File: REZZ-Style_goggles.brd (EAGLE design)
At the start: 65.5 x 65.5 mm, 85 parts

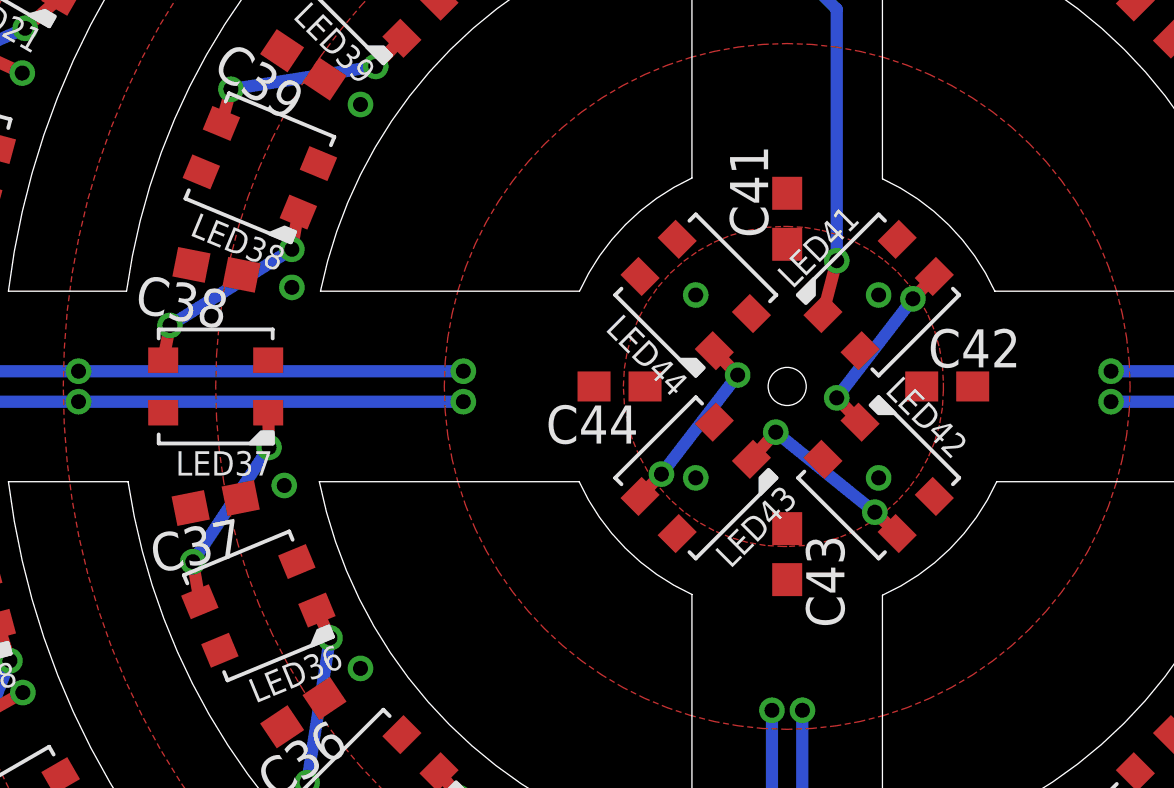
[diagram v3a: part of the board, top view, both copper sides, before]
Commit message: revised placements to improve pours
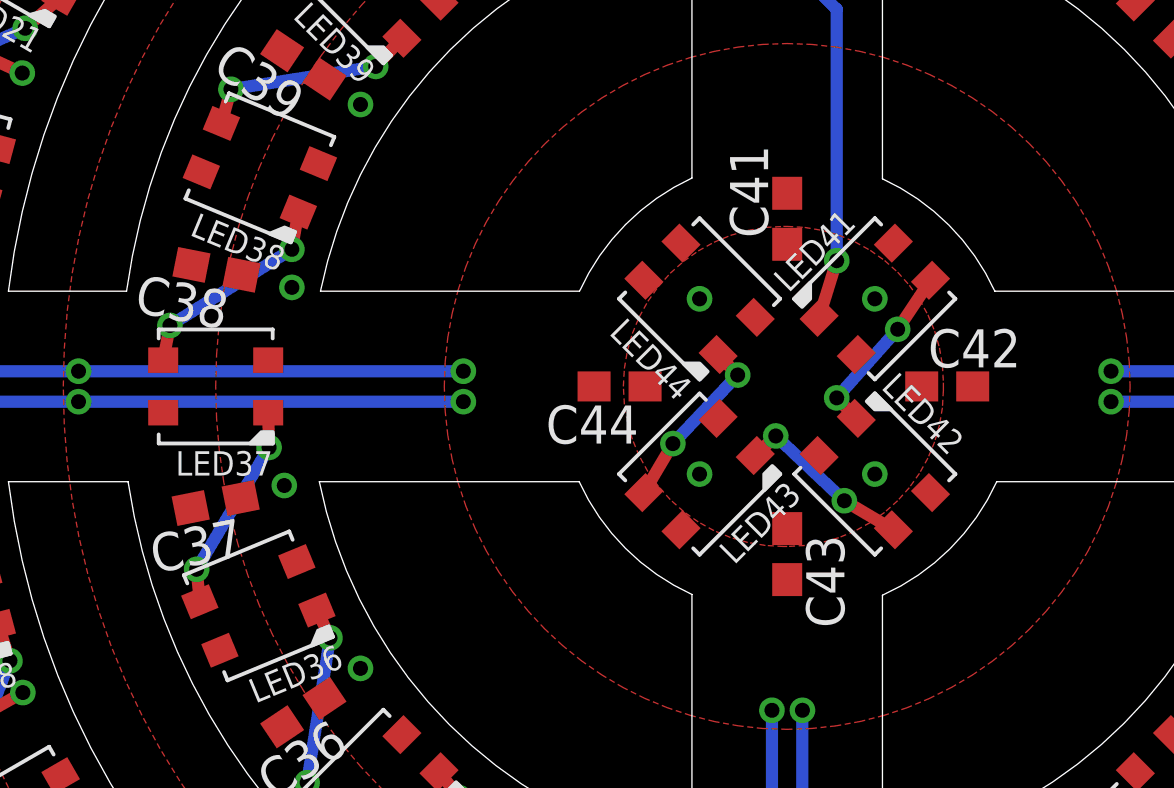
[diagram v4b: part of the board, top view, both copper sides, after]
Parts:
- moved LED43 0.18 mm to (30.1, 32.6)
- moved LED42 0.18 mm to (35.9, 32.6)
- moved LED44 0.18 mm to (30.1, 38.5)
- moved LED41 0.18 mm to (35.9, 38.5)
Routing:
- net N$44: track 6.49 -> 5.99 mm
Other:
- board text removed: "Data Out"
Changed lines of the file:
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@@
 <text x="44.1452" y="7.366" size="1.016" layer="21" ratio="10">G</text>
 <text x="29.7942" y="5.334" size="1.016" layer="21" ratio="10" rot="R90">PWR</text>
-<text x="22.352" y="61.214" size="1.016" layer="22" ratio="10" rot="MR0">Data
-Out</text>
 <text x="38.608" y="63.5" size="1.016" layer="22" ratio="10" rot="MR0">Data
 Input</text>
@@
 <wire x1="29.845" y1="9.6012" x2="7.0612" y2="32.385" width="0.0254" layer="20" curve="-76.053667"/>
 <wire x1="29.845" y1="13.6906" x2="11.049" y2="32.385" width="0.0254" layer="20" curve="-73.212053"/>
-<hole x="33.02" y="35.56" drill="1.27"/>
 <wire x1="17.4625" y1="38.735" x2="26.0858" y2="38.735" width="0.0254" layer="20"/>
 <wire x1="48.6029" y1="38.735" x2="39.9415" y2="38.735" width="0.0254" layer="20"/>
@@
 </class>
 </classes>
-<designrules name="oshpark-2layer">
+<designrules name="oshpark-2layer *">
 <description language="de">&lt;b&gt;EAGLE Design Rules&lt;/b&gt;
 &lt;p&gt;
@@
 <param name="mlMinCreamFrame" value="0mil"/>
 <param name="mlMaxCreamFrame" value="0mil"/>
-<param name="mlViaStopLimit" value="0mil"/>
+<param name="mlViaStopLimit" value="20mil"/>
 <param name="srRoundness" value="0"/>
 <param name="srMinRoundness" value="0mil"/>
@@
 <element name="C39" library="rcl" package="C0603" value="" x="16.891" y="46.2788" rot="R146.3"/>
 <element name="C40" library="rcl" package="C0603" value="" x="22.2504" y="51.4858" rot="R123.8"/>
-<element name="LED41" library="adafruit" package="LED3535" value="WS2812B3535" x="36.068" y="38.608" rot="R45"/>
-<element name="LED42" library="adafruit" package="LED3535" value="WS2812B3535" x="36.068" y="32.512" rot="R315"/>
-<element name="LED43" library="adafruit" package="LED3535" value="WS2812B3535" x="29.972" y="32.512" rot="R225"/>
-<element name="LED44" library="adafruit" package="LED3535" value="WS2812B3535" x="29.972" y="38.608" rot="R135"/>
+<element name="LED41" library="adafruit" package="LED3535" value="WS2812B3535" x="35.941" y="38.481" rot="R45"/>
+<element name="LED42" library="adafruit" package="LED3535" value="WS2812B3535" x="35.941" y="32.639" rot="R315"/>
+<element name="LED43" library="adafruit" package="LED3535" value="WS2812B3535" x="30.099" y="32.639" rot="R225"/>
+<element name="LED44" library="adafruit" package="LED3535" value="WS2812B3535" x="30.099" y="38.481" rot="R135"/>
 <element name="C41" library="rcl" package="C0603" value="" x="33.02" y="41.148" rot="R90"/>
 <element name="C42" library="rcl" package="C0603" value="" x="38.354" y="35.56"/>
@@
 <wire x1="9.398" y1="36.068" x2="22.225" y2="36.068" width="0.4064" layer="16"/>
 <wire x1="9.398" y1="35.052" x2="22.225" y2="35.052" width="0.4064" layer="16"/>
-<wire x1="36.686715625" y1="40.464153125" x2="39.204" y2="35.56" width="0" layer="19" extent="1-1"/>
 </signal>
 <signal name="VDD">
@@
 <vertex x="32.893" y="30.226" curve="-90"/>
 </polygon>
-<via x="29.972" y="32.512" extent="1-16" drill="0.5"/>
-<via x="29.972" y="38.608" extent="1-16" drill="0.5"/>
-<via x="36.068" y="32.512" extent="1-16" drill="0.5"/>
-<via x="36.068" y="38.608" extent="1-16" drill="0.5"/>
+<via x="30.099" y="32.639" extent="1-16" drill="0.5"/>
+<via x="30.099" y="38.481" extent="1-16" drill="0.5"/>
+<via x="35.941" y="32.639" extent="1-16" drill="0.5"/>
+<via x="35.941" y="38.481" extent="1-16" drill="0.5"/>
 <via x="30.861" y="49.53" extent="1-16" drill="0.5"/>
 <via x="35.179" y="49.53" extent="1-16" drill="0.5"/>
@@
 <contactref element="LED36" pad="3"/>
 <contactref element="LED37" pad="1"/>
-<via x="13.208" y="29.718" extent="1-16" drill="0.5"/>
+<via x="13.335" y="29.464" extent="1-16" drill="0.5"/>
 <via x="15.748" y="33.528" extent="1-16" drill="0.5"/>
-<wire x1="13.4407625" y1="28.383496875" x2="13.208" y2="29.718" width="0.4064" layer="1"/>
+<wire x1="13.4407625" y1="28.383496875" x2="13.335" y2="29.464" width="0.4064" layer="1"/>
 <wire x1="15.72" y1="34.685" x2="15.748" y2="33.528" width="0.4064" layer="1"/>
-<wire x1="13.208" y1="29.718" x2="15.748" y2="33.528" width="0.4064" layer="16"/>
+<wire x1="13.335" y1="29.464" x2="15.748" y2="33.528" width="0.4064" layer="16"/>
 </signal>
 <signal name="N$39">
@@
 <via x="27.051" y="55.753" extent="1-16" drill="0.5"/>
 <via x="34.671" y="39.751" extent="1-16" drill="0.5"/>
-<wire x1="34.21184375" y1="37.98928125" x2="34.671" y2="39.751" width="0.4064" layer="1"/>
+<wire x1="34.08484375" y1="37.86228125" x2="34.671" y2="39.751" width="0.4064" layer="1"/>
 <wire x1="25.843496875" y1="55.139234375" x2="27.051" y2="55.753" width="0.4064" layer="1"/>
 <wire x1="34.671" y1="39.751" x2="34.671" y2="48.133" width="0.4064" layer="16"/>
@@
 <contactref element="LED42" pad="1"/>
 <via x="34.671" y="35.179" extent="1-16" drill="0.5"/>
-<via x="37.211" y="38.481" extent="1-16" drill="0.5"/>
-<wire x1="37.211" y1="38.481" x2="34.671" y2="35.179" width="0.4064" layer="16"/>
-<wire x1="37.211" y1="38.481" x2="37.924153125" y2="39.226715625" width="0.4064" layer="1"/>
-<wire x1="34.671" y1="35.179" x2="35.44928125" y2="34.368153125" width="0.4064" layer="1"/>
+<via x="36.703" y="37.465" extent="1-16" drill="0.5"/>
+<wire x1="36.703" y1="37.465" x2="34.671" y2="35.179" width="0.4064" layer="16"/>
+<wire x1="36.703" y1="37.465" x2="37.797153125" y2="39.099715625" width="0.4064" layer="1"/>
+<wire x1="34.671" y1="35.179" x2="35.32228125" y2="34.495153125" width="0.4064" layer="1"/>
 </signal>
 <signal name="N$44">
 <contactref element="LED42" pad="3"/>
 <contactref element="LED43" pad="1"/>
-<via x="35.941" y="31.369" extent="1-16" drill="0.5"/>
-<via x="32.639" y="34.036" extent="1-16" drill="0.5"/>
-<wire x1="35.941" y1="31.369" x2="32.639" y2="34.036" width="0.4064" layer="16"/>
-<wire x1="36.686715625" y1="30.65584375" x2="35.941" y2="31.369" width="0.4064" layer="1"/>
-<wire x1="31.828153125" y1="33.130715625" x2="32.639" y2="34.036" width="0.4064" layer="1"/>
+<via x="34.925" y="31.75" extent="1-16" drill="0.5"/>
+<via x="32.639" y="33.909" extent="1-16" drill="0.5"/>
+<wire x1="34.925" y1="31.75" x2="32.639" y2="33.909" width="0.4064" layer="16"/>
+<wire x1="36.559715625" y1="30.78284375" x2="34.925" y2="31.75" width="0.4064" layer="1"/>
+<wire x1="31.955153125" y1="33.257715625" x2="32.639" y2="33.909" width="0.4064" layer="1"/>
 </signal>
 <signal name="N$45">
 <contactref element="LED43" pad="3"/>
 <contactref element="LED44" pad="1"/>
-<via x="28.829" y="32.639" extent="1-16" drill="0.5"/>
+<via x="29.21" y="33.655" extent="1-16" drill="0.5"/>
 <via x="31.369" y="35.941" extent="1-16" drill="0.5"/>
-<wire x1="28.829" y1="32.639" x2="31.369" y2="35.941" width="0.4064" layer="16"/>
-<wire x1="28.829" y1="32.639" x2="28.11584375" y2="31.89328125" width="0.4064" layer="1"/>
-<wire x1="30.590715625" y1="36.75184375" x2="31.369" y2="35.941" width="0.4064" layer="1"/>
+<wire x1="29.21" y1="33.655" x2="31.369" y2="35.941" width="0.4064" layer="16"/>
+<wire x1="29.21" y1="33.655" x2="28.24284375" y2="32.02028125" width="0.4064" layer="1"/>
+<wire x1="30.717715625" y1="36.62484375" x2="31.369" y2="35.941" width="0.4064" layer="1"/>
 </signal>
 </signals>
